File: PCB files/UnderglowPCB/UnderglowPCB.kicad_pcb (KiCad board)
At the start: 4 copper layers, 90 x 65 mm, 71 parts, among them J1 Conn_01x03, J10 Conn_01x03, J11 Conn_01x05, J12 Conn_01x07, J2 DB9_Male, J3 USB_B_Micro, J4 Conn_01x03, J5 Conn_01x03, J6 Conn_01x03, J7 Conn_01x03, J8 Conn_01x03, J9 Conn_01x03, Q1 S8050, Q2 S8050, U1 ESP32-WROOM-32D, U2 LMR14030-Q1, U3 NCP1117-3.3_SOT223, U4 TXB0108DQSR, U6 SN65HVD230, U7 USBLC6-2SC6, U8 CP2102N-A01-GQFN28

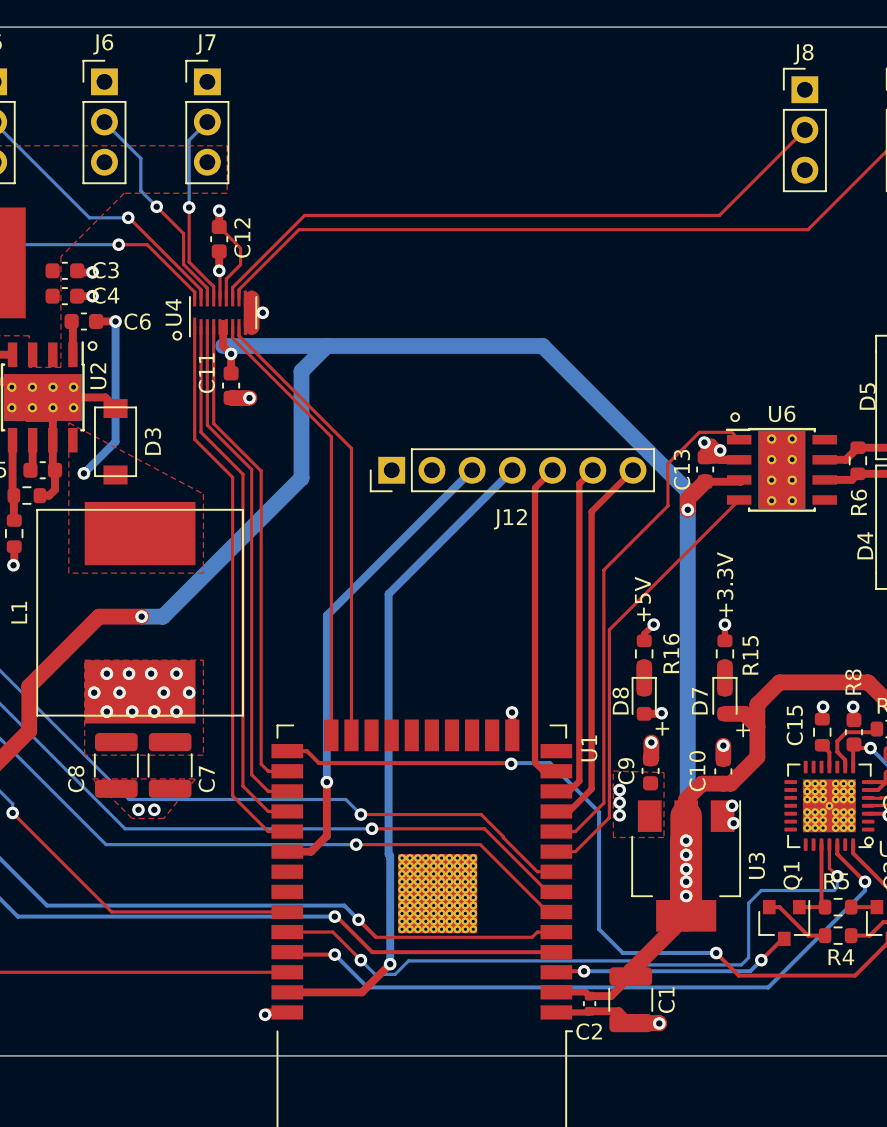
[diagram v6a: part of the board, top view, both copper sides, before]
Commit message: PCB data updated, 1.3.2 ordering information is provided.
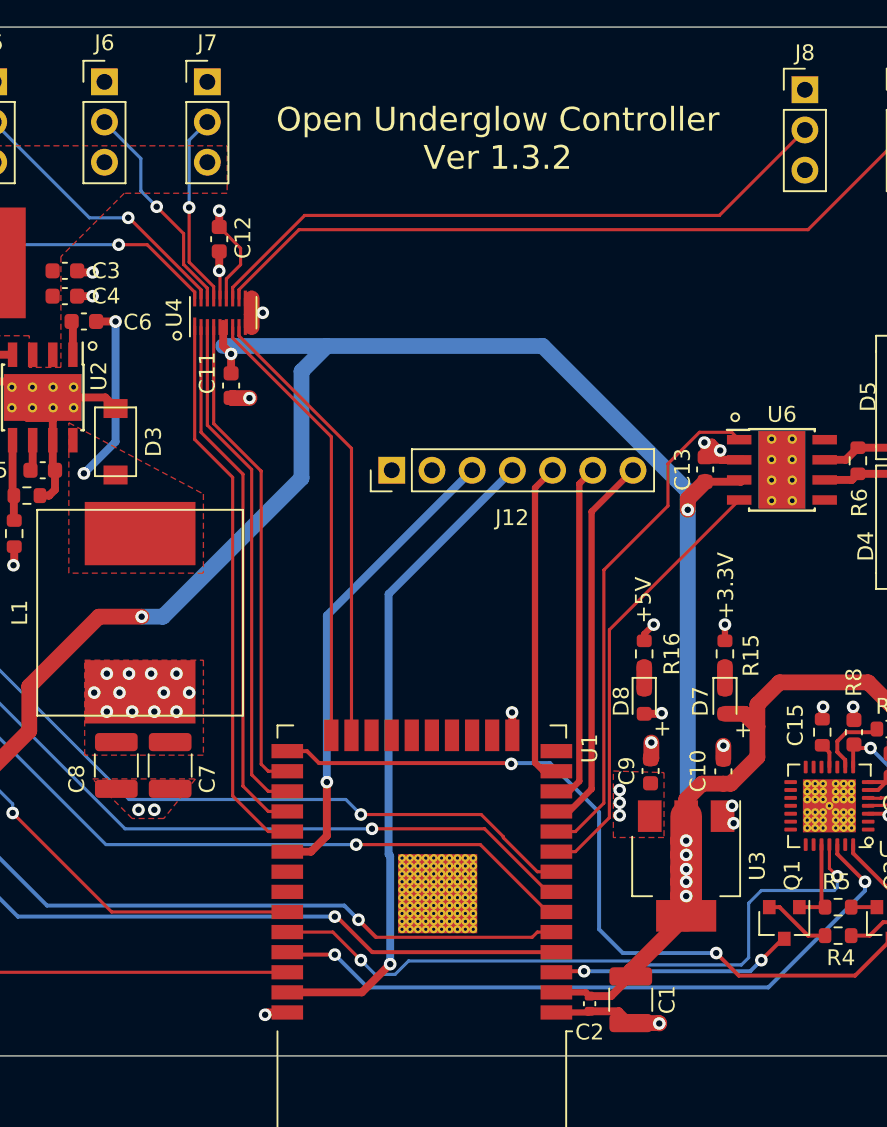
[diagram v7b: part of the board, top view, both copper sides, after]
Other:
- board text added: "Open Underglow Controller Ver 1.3.2"
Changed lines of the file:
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@@
   (general
     (thickness 1.6)
-    (drawings 43)
+    (drawings 44)
     (tracks 564)
     (zones 0)
@@
   )
   (setup
-    (last_trace_width 0.5)
+    (last_trace_width 0.4)
     (user_trace_width 0.15)
     (user_trace_width 0.2)
@@
       (outputformat 1)
       (mirror false)
-      (drillshape 1)
+      (drillshape 0)
       (scaleselection 1)
-      (outputdirectory ""))
+      (outputdirectory "Drill files/"))
   )
   (net 0 "")
@@
       (effects (font (size 1 1) (thickness 0.15)))
     )
-    (fp_text user %R (at 0 0 90) (layer F.Fab)
-      (effects (font (size 0.8 0.8) (thickness 0.12)))
-    )
     (fp_line (start -1.6 1.25) (end -1.6 -1.25) (layer F.Fab) (width 0.1))
     (fp_line (start -1.6 -1.25) (end 1.6 -1.25) (layer F.Fab) (width 0.1))
@@
     (fp_line (start 2.3 -1.6) (end 2.3 1.6) (layer F.CrtYd) (width 0.05))
     (fp_line (start 2.3 1.6) (end -2.3 1.6) (layer F.CrtYd) (width 0.05))
-    (pad 2 smd roundrect (at 1.475 0 270) (size 1.15 2.7) (layers F.Cu F.Paste F.Mask) (roundrect_rratio 0.217391)
+    (fp_text user %R (at 0 0 90) (layer F.Fab)
+      (effects (font (size 0.8 0.8) (thickness 0.12)))
+    )
+    (pad 2 smd roundrect (at 1.475 0 270) (size 1.15 2.7) (layers F.Cu F.Paste F.Mask) (roundrect_rratio 0.2173904347826087)
       (net 2 GND))
-    (pad 1 smd roundrect (at -1.475 0 270) (size 1.15 2.7) (layers F.Cu F.Paste F.Mask) (roundrect_rratio 0.217391)
+    (pad 1 smd roundrect (at -1.475 0 270) (size 1.15 2.7) (layers F.Cu F.Paste F.Mask) (roundrect_rratio 0.2173904347826087)
       (net 6 +3V3))
     (model ${KISYS3DMOD}/Capacitor_SMD.3dshapes/C_1210_3225Metric.wrl
@@
       (effects (font (size 0.8 0.8) (thickness 0.12)))
     )
-    (pad 2 smd roundrect (at 1.475 0 270) (size 1.15 2.7) (layers F.Cu F.Paste F.Mask) (roundrect_rratio 0.217391)
+    (pad 2 smd roundrect (at 1.475 0 270) (size 1.15 2.7) (layers F.Cu F.Paste F.Mask) (roundrect_rratio 0.2173904347826087)
       (net 2 GND))
-    (pad 1 smd roundrect (at -1.475 0 270) (size 1.15 2.7) (layers F.Cu F.Paste F.Mask) (roundrect_rratio 0.217391)
+    (pad 1 smd roundrect (at -1.475 0 270) (size 1.15 2.7) (layers F.Cu F.Paste F.Mask) (roundrect_rratio 0.2173904347826087)
       (net 7 +5V))
     (model ${KISYS3DMOD}/Capacitor_SMD.3dshapes/C_1210_3225Metric.wrl
@@
       (effects (font (size 0.8 0.8) (thickness 0.12)))
     )
-    (pad 1 smd roundrect (at -1.475 0 270) (size 1.15 2.7) (layers F.Cu F.Paste F.Mask) (roundrect_rratio 0.217391)
+    (pad 1 smd roundrect (at -1.475 0 270) (size 1.15 2.7) (layers F.Cu F.Paste F.Mask) (roundrect_rratio 0.2173904347826087)
       (net 7 +5V))
-    (pad 2 smd roundrect (at 1.475 0 270) (size 1.15 2.7) (layers F.Cu F.Paste F.Mask) (roundrect_rratio 0.217391)
+    (pad 2 smd roundrect (at 1.475 0 270) (size 1.15 2.7) (layers F.Cu F.Paste F.Mask) (roundrect_rratio 0.2173904347826087)
       (net 2 GND))
     (model ${KISYS3DMOD}/Capacitor_SMD.3dshapes/C_1210_3225Metric.wrl
@@
       (solder_mask_margin 0.0508))
   )
+  (gr_text "Open Underglow Controller\nVer 1.3.2\n" (at 154.65 75) (layer F.SilkS)
+    (effects (font (size 1.5 1.5) (thickness 0.2)))
+  )
   (gr_circle (center 134.4 87.45) (end 134.65 87.45) (layer F.SilkS) (width 0.12))
   (gr_text "12V ONLY" (at 125.8 80.65) (layer B.SilkS)
@@
     (effects (font (size 1 1) (thickness 0.15)) (justify mirror))
   )
-  (via (at 164.85 130.9) (size 0.8) (drill 0.4) (layers F.Cu B.Cu) (net 2))
   (segment (start 108.415 97.29) (end 108.375 97.25) (width 0.5) (layer F.Cu) (net 1))
   (segment (start 111.1 97.29) (end 108.415 97.29) (width 0.5) (layer F.Cu) (net 1))
@@
   (segment (start 112.6 96.75) (end 113.775 96.75) (width 0.5) (layer F.Cu) (net 1))
   (segment (start 112.06 97.29) (end 112.6 96.75) (width 0.5) (layer F.Cu) (net 1))
+  (via (at 164.85 130.9) (size 0.8) (drill 0.4) (layers F.Cu B.Cu) (net 2))
   (via (at 139.95 130.35) (size 0.8) (drill 0.4) (layers F.Cu B.Cu) (net 2))
   (via (at 155.55 111.25) (size 0.8) (drill 0.4) (layers F.Cu B.Cu) (net 2))
@@
   (segment (start 166.65 122.75) (end 166.55 122.85) (width 1) (layer B.Cu) (net 6))
   (segment (start 166.65 98.45) (end 166.65 122.75) (width 1) (layer B.Cu) (net 6))
-  (via (at 162.35 117.75) (size 0.8) (drill 0.4) (layers F.Cu B.Cu) (net 7))
-  (via (at 162.35 116.95) (size 0.8) (drill 0.4) (layers F.Cu B.Cu) (net 7))
-  (via (at 162.35 116.15) (size 0.8) (drill 0.4) (layers F.Cu B.Cu) (net 7))
-  (via (at 124.05 101.95) (size 0.8) (drill 0.4) (layers F.Cu B.Cu) (net 7))
-  (via (at 131.35 108.8) (size 0.8) (drill 0.4) (layers F.Cu B.Cu) (net 7))
-  (via (at 132.75 108.8) (size 0.8) (drill 0.4) (layers F.Cu B.Cu) (net 7))
-  (via (at 132.95 111.2) (size 0.8) (drill 0.4) (layers F.Cu B.Cu) (net 7))
-  (via (at 131.55 111.2) (size 0.8) (drill 0.4) (layers F.Cu B.Cu) (net 7))
-  (via (at 130.75 110) (size 0.8) (drill 0.4) (layers F.Cu B.Cu) (net 7))
-  (via (at 129.95 108.8) (size 0.8) (drill 0.4) (layers F.Cu B.Cu) (net 7))
-  (via (at 129.95 111.2) (size 0.8) (drill 0.4) (layers F.Cu B.Cu) (net 7))
-  (via (at 129.15 110) (size 0.8) (drill 0.4) (layers F.Cu B.Cu) (net 7))
-  (via (at 133.55 110) (size 0.8) (drill 0.4) (layers F.Cu B.Cu) (net 7))
-  (via (at 135.15 110) (size 0.8) (drill 0.4) (layers F.Cu B.Cu) (net 7))
-  (via (at 134.35 108.8) (size 0.8) (drill 0.4) (layers F.Cu B.Cu) (net 7))
-  (via (at 134.35 111.2) (size 0.8) (drill 0.4) (layers F.Cu B.Cu) (net 7))
-  (via (at 165 111.3) (size 0.8) (drill 0.4) (layers F.Cu B.Cu) (net 7))
-  (segment (start 164.9625 111.3375) (end 165 111.3) (width 0.5) (layer F.Cu) (net 7))
-  (segment (start 163.9 111.3375) (end 164.9625 111.3375) (width 0.5) (layer F.Cu) (net 7))
-  (segment (start 183.55 119.9) (end 182.6 119.9) (width 1) (layer F.Cu) (net 7))
-  (via (at 182.6 119.9) (size 0.8) (drill 0.4) (layers F.Cu B.Cu) (net 7))
   (segment (start 137.8 89.825) (end 137.8 89.840002) (width 0.5) (layer F.Cu) (net 6))
   (segment (start 137.8 89.825) (end 137.8 88.6) (width 0.5) (layer F.Cu) (net 6))
@@
   (segment (start 161.805 129.17) (end 163.05 127.925) (width 0.5) (layer F.Cu) (net 6))
   (segment (start 160.45 129.17) (end 161.805 129.17) (width 0.5) (layer F.Cu) (net 6))
+  (via (at 162.35 117.75) (size 0.8) (drill 0.4) (layers F.Cu B.Cu) (net 7))
+  (via (at 162.35 116.95) (size 0.8) (drill 0.4) (layers F.Cu B.Cu) (net 7))
+  (via (at 162.35 116.15) (size 0.8) (drill 0.4) (layers F.Cu B.Cu) (net 7))
+  (via (at 124.05 101.95) (size 0.8) (drill 0.4) (layers F.Cu B.Cu) (net 7))
+  (via (at 131.35 108.8) (size 0.8) (drill 0.4) (layers F.Cu B.Cu) (net 7))
+  (via (at 132.75 108.8) (size 0.8) (drill 0.4) (layers F.Cu B.Cu) (net 7))
+  (via (at 132.95 111.2) (size 0.8) (drill 0.4) (layers F.Cu B.Cu) (net 7))
+  (via (at 131.55 111.2) (size 0.8) (drill 0.4) (layers F.Cu B.Cu) (net 7))
+  (via (at 130.75 110) (size 0.8) (drill 0.4) (layers F.Cu B.Cu) (net 7))
+  (via (at 129.95 108.8) (size 0.8) (drill 0.4) (layers F.Cu B.Cu) (net 7))
+  (via (at 129.95 111.2) (size 0.8) (drill 0.4) (layers F.Cu B.Cu) (net 7))
+  (via (at 129.15 110) (size 0.8) (drill 0.4) (layers F.Cu B.Cu) (net 7))
+  (via (at 133.55 110) (size 0.8) (drill 0.4) (layers F.Cu B.Cu) (net 7))
+  (via (at 135.15 110) (size 0.8) (drill 0.4) (layers F.Cu B.Cu) (net 7))
+  (via (at 134.35 108.8) (size 0.8) (drill 0.4) (layers F.Cu B.Cu) (net 7))
+  (via (at 134.35 111.2) (size 0.8) (drill 0.4) (layers F.Cu B.Cu) (net 7))
+  (via (at 165 111.3) (size 0.8) (drill 0.4) (layers F.Cu B.Cu) (net 7))
+  (segment (start 164.9625 111.3375) (end 165 111.3) (width 0.5) (layer F.Cu) (net 7))
+  (segment (start 163.9 111.3375) (end 164.9625 111.3375) (width 0.5) (layer F.Cu) (net 7))
+  (segment (start 183.55 119.9) (end 182.6 119.9) (width 1) (layer F.Cu) (net 7))
+  (via (at 182.6 119.9) (size 0.8) (drill 0.4) (layers F.Cu B.Cu) (net 7))
   (segment (start 124.1 101.9) (end 124.05 101.95) (width 0.5) (layer F.Cu) (net 7))
   (segment (start 124.1 100.775) (end 124.1 101.9) (width 0.5) (layer F.Cu) (net 7))
